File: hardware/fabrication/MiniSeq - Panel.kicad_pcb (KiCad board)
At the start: 2 copper layers, 80 x 128.5 mm, 14 parts

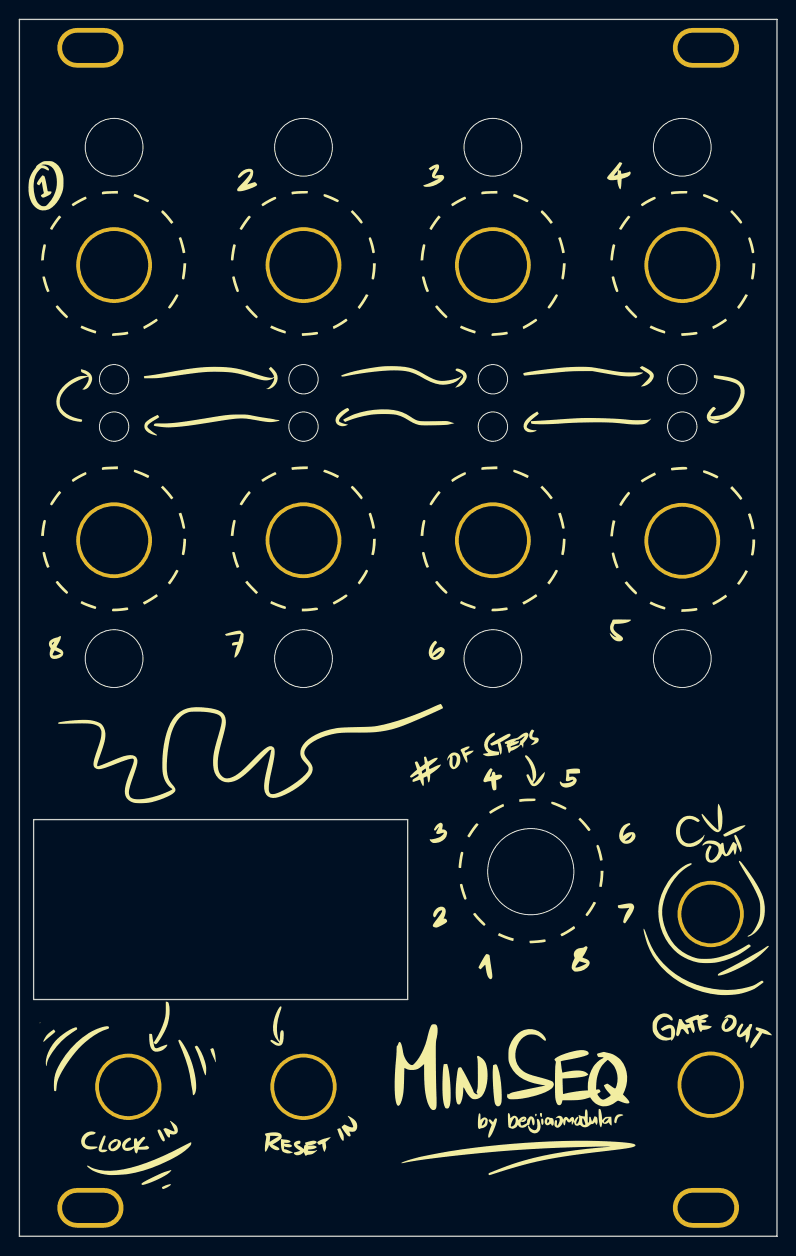
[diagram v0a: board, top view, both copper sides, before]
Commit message: Added copper fills to panel
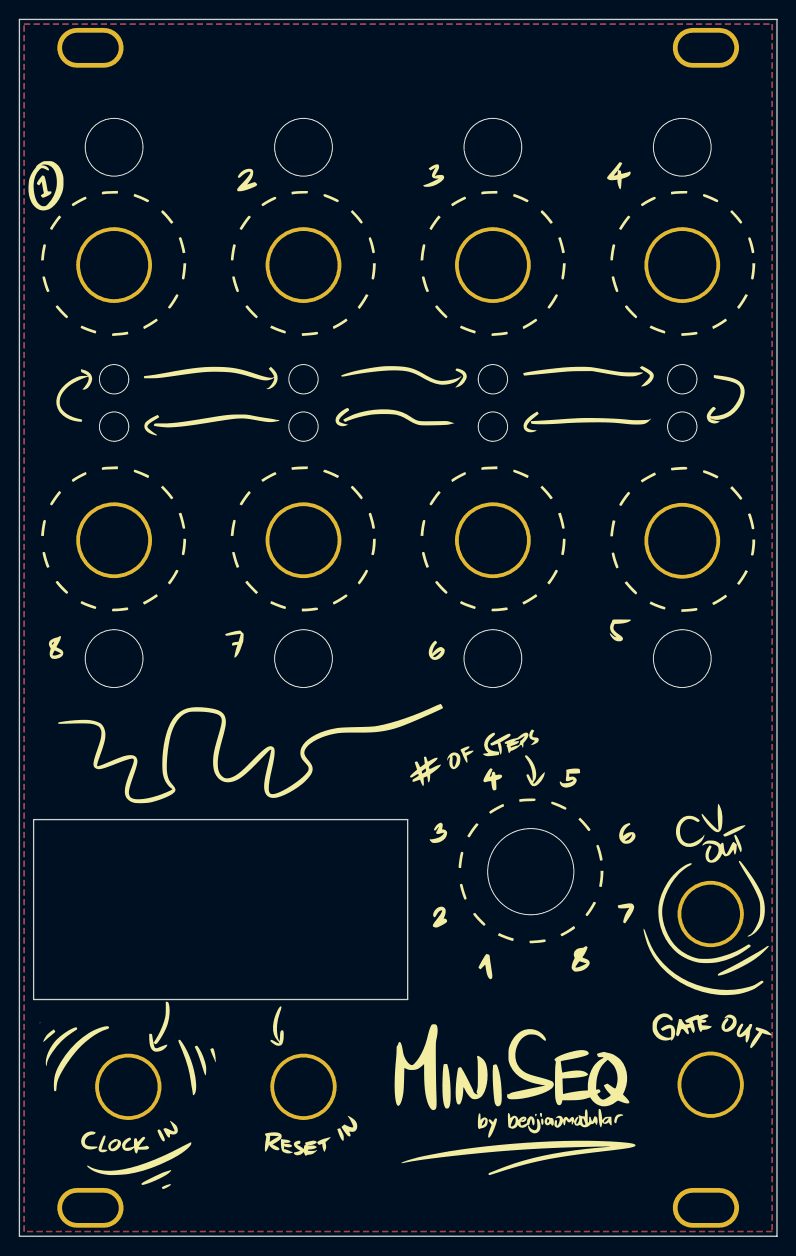
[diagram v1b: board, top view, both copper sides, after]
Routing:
- added copper zone on B.Cu, net (none)
- added copper zone on F.Cu, net (none)
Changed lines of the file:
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@@
 		(net 0)
 	)
+	(zone
+		(net 0)
+		(net_name "")
+		(layer "F.Cu")
+		(hatch edge 0.5)
+		(connect_pads
+			(clearance 0.5)
+		)
+		(min_thickness 0.25)
+		(filled_areas_thickness no)
+		(fill yes
+			(thermal_gap 0.5)
+			(thermal_bridge_width 0.5)
+			(island_removal_mode 1)
+			(island_area_min 10)
+		)
+		(polygon
+			(pts
+				(xy 50.5 30.5) (xy 129.5 30.5) (xy 129.5 158) (xy 50.5 158)
+			)
+		)
+	)
+	(zone
+		(net 0)
+		(net_name "")
+		(layer "B.Cu")
+		(hatch edge 0.5)
+		(priority 1)
+		(connect_pads
+			(clearance 0.5)
+		)
+		(min_thickness 0.25)
+		(filled_areas_thickness no)
+		(fill yes
+			(thermal_gap 0.5)
+			(thermal_bridge_width 0.5)
+			(island_removal_mode 1)
+			(island_area_min 10)
+		)
+		(polygon
+			(pts
+				(xy 50.5 30.5) (xy 129.5 30.5) (xy 129.5 158) (xy 50.5 158)
+			)
+		)
+	)
 )
